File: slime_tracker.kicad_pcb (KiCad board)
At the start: 2 copper layers, 35 x 42.5 mm, 25 parts, among them CN1 SM05B-SRSS-TB (LF)(SN), SW1 MK-12C02-G020, U1 ICM-45686, U2 QMC6309, Y1 1532H-24.000JWVDTL

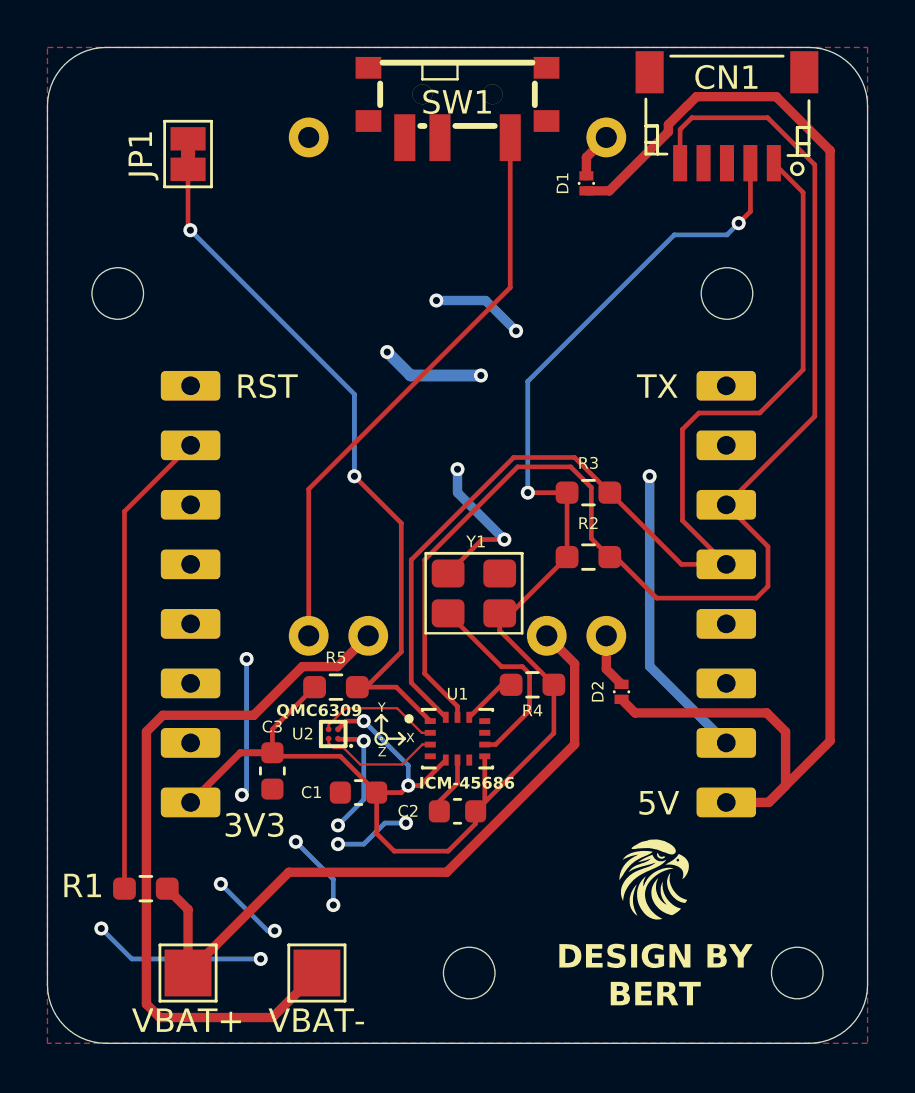
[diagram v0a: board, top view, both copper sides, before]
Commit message: Converted from global to project libraries
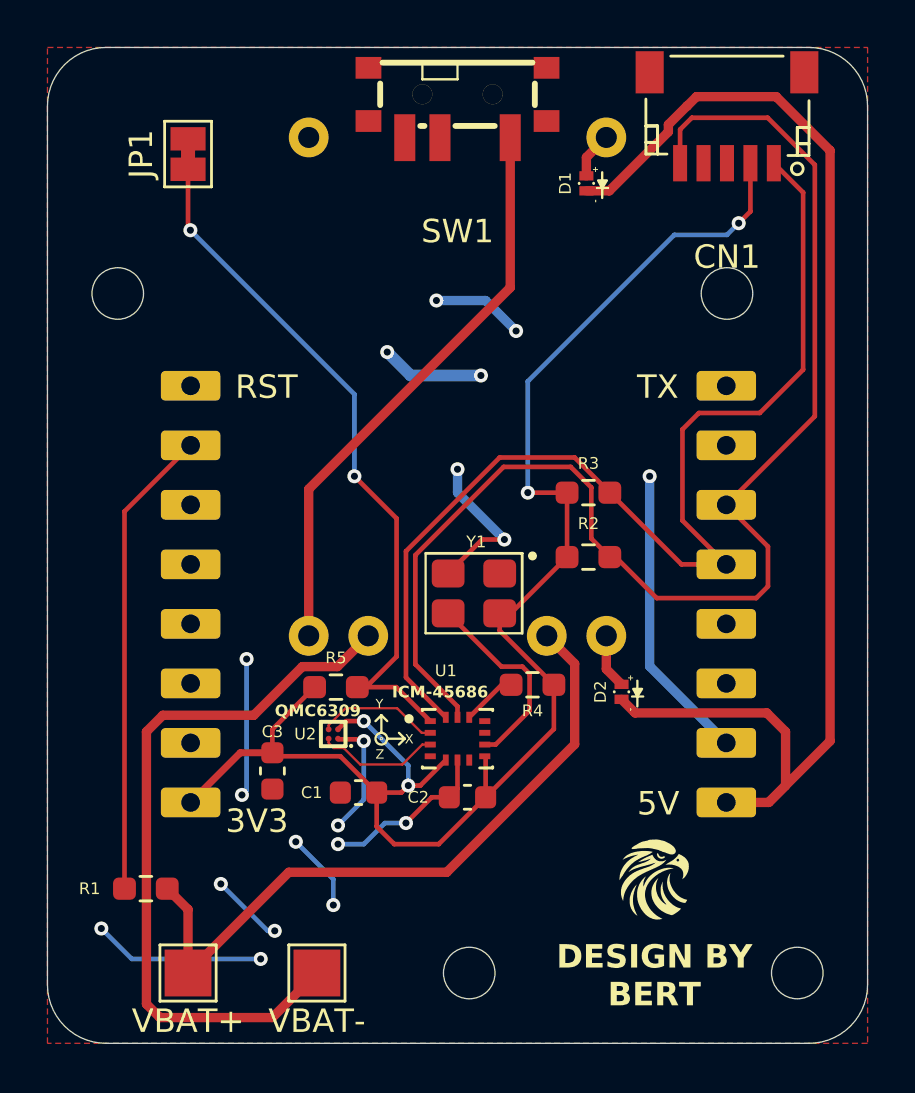
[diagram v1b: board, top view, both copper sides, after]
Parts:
- CN1: footprint Personal:CONN-SMD_SM05B-SRSS-TB-LF-SN -> Bert-Slime-PCB:CONN-SMD_SM05B-SRSS-TB-LF-SN
- D1, D2: footprint PMEG3010ESBYL:SOD993_L1.0-W0.6-LS1.0-RD -> Bert-Slime-PCB:SOD993_L1.0-W0.6-LS1.0-RD
- SW1: footprint Personal:SW-SMD_MK-12C02-G020 -> Bert-Slime-PCB:SW-SMD_MK-12C02-G020
- U1: footprint ICM_45686:IC_ICM-45686 -> Bert-Slime-PCB:IC_ICM-45686
- U2: footprint QMC6309-lib:X1-WLB0808-4_L0.8-W0.8-P0.40-TL -> Bert-Slime-PCB:X1-WLB0808-4_L0.8-W0.8-P0.40-TL
- U3: footprint Personal:D1-Mini -> Bert-Slime-PCB:D1-Mini
- U4: footprint Personal:TP4056-USBC-MODULE -> Bert-Slime-PCB:TP4056-USBC-MODULE
- moved C2 0.74 mm to (140.4, 102.0)
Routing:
- net +3V3: track 69.5 -> 68.0 mm
- net GND: track 58.6 -> 60.1 mm
- net SCL: track 55.9 -> 56.6 mm
- net SDA: track 46.5 -> 47.1 mm
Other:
- board text added: "ICM-45686"
- board text added: "QMC6309"
